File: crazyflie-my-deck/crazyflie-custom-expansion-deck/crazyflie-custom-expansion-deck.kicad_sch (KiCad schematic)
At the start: 3 parts, among them J1 Conn_01x10, J2 Conn_02x10_Odd_Even, J3 Conn_01x10

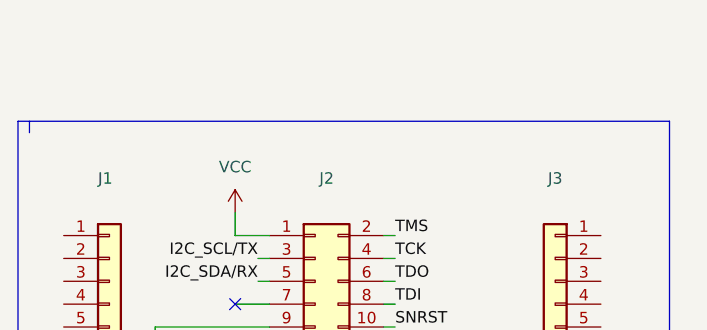
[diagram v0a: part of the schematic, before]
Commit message: [add] boost voltage
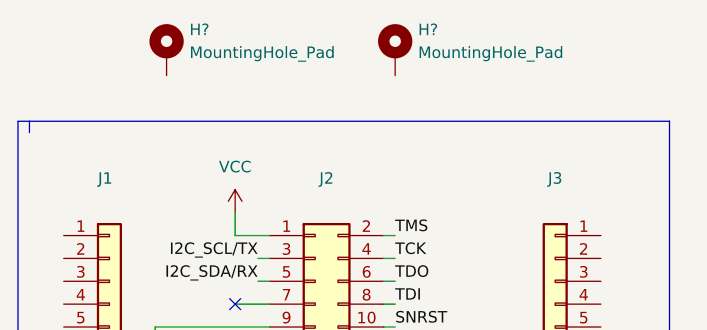
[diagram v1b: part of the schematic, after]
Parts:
- added H? (x2): MountingHole_Pad, symbol Mechanical:MountingHole_Pad
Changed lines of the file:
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@@
+    (pin "1")
+  )
+  (symbol (lib_id "Mechanical:MountingHole_Pad") (at 151.13 66.04 0) (unit 1)
+    (in_bom yes) (on_board yes) (fields_autoplaced)
+    (property "Reference" "H?" (id 0) (at 153.67 63.4999 0)
+      (effects (font (size 1.27 1.27)) (justify left))
+    )
+    (property "Value" "MountingHole_Pad" (id 1) (at 153.67 66.0399 0)
+      (effects (font (size 1.27 1.27)) (justify left))
+    )
+    (property "Footprint" "" (id 2) (at 151.13 66.04 0)
+      (effects (font (size 1.27 1.27)) hide)
+    )
+    (property "Datasheet" "~" (id 3) (at 151.13 66.04 0)
+      (effects (font (size 1.27 1.27)) hide)
+    )
     (pin "1")
   )
@@
     (pin "1")
   )
+  (symbol (lib_id "Mechanical:MountingHole_Pad") (at 125.73 66.04 0) (unit 1)
+    (in_bom yes) (on_board yes) (fields_autoplaced)
+    (property "Reference" "H?" (id 0) (at 128.27 63.4999 0)
+      (effects (font (size 1.27 1.27)) (justify left))
+    )
+    (property "Value" "MountingHole_Pad" (id 1) (at 128.27 66.0399 0)
+      (effects (font (size 1.27 1.27)) (justify left))
+    )
+    (property "Footprint" "" (id 2) (at 125.73 66.04 0)
+      (effects (font (size 1.27 1.27)) hide)
+    )
+    (property "Datasheet" "~" (id 3) (at 125.73 66.04 0)
+      (effects (font (size 1.27 1.27)) hide)
+    )
+    (pin "1")
+  )
   (sheet_instances
     (path "/" (page "1"))
@@
       (reference "#PWR06") (unit 1) (value "GNDA") (footprint "")
     )
+    (path "/76a03ed3-762f-4d41-a0c5-8ca717b403a8"
+      (reference "H?") (unit 1) (value "MountingHole_Pad") (footprint "")
+    )
+    (path "/d9a65ee8-bd3a-49dd-a674-f61b61978027"
+      (reference "H?") (unit 1) (value "MountingHole_Pad") (footprint "")
+    )
     (path "/388ad4a6-c2ab-454b-ae40-8bf09ddb6eea"

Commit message: acomodo de componentes
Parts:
- removed J2: Conn_02x10_Odd_Even, Connector_PinHeader_1.27mm:PinHeader_2x10_P1.27mm_Vertical, symbol Connector_Generic:Conn_02x10_Odd_Even
- added C1, C4: C_Polarized, Capacitor_Tantalum_SMD:CP_EIA-3528-15_AVX-H, symbol Device:C_Polarized
- added C2: C_Polarized, Capacitor_SMD:C_0805_2012Metric, symbol Device:C_Polarized
- added C3: C_Polarized, Capacitor_SMD:C_1210_3225Metric, symbol Device:C_Polarized
- added D1: 1SS355VM, Diode_SMD:D_SOD-323F, symbol Diode:1SS355VM
- added J2: Conn_01x06_Male, Connector_PinHeader_1.27mm:PinHeader_1x06_P1.27mm_Horizontal, symbol Connector:Conn_01x06_Male
- added L1: L, Inductor_SMD:L_1210_3225Metric, symbol Device:L
- added R1, R2, R3, R4: R, Resistor_SMD:R_0805_2012Metric, symbol Device:R
- added U1: MAX712CSE, Package_SO:SOIC-16_3.9x9.9mm_P1.27mm, symbol Battery_Management:MAX712CSE
- gave numbers to parts that had none: 2
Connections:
- net GND: now also C1.2, C2.2, C3.2, C4.2, J2.2 (Pin_2), R2.2, R4.2
- new net: R3.2, R4.1
- new net: C1.1, J2.1 (Pin_1), L1.1, R1.1
- new net: D1.2 (A), L1.2
- new net: R1.2, R2.1
- new net: C4.1, D1.1 (K)
- no-connect marks 1 -> 0
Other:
- moved on the sheet: H1, H2, J1, J3

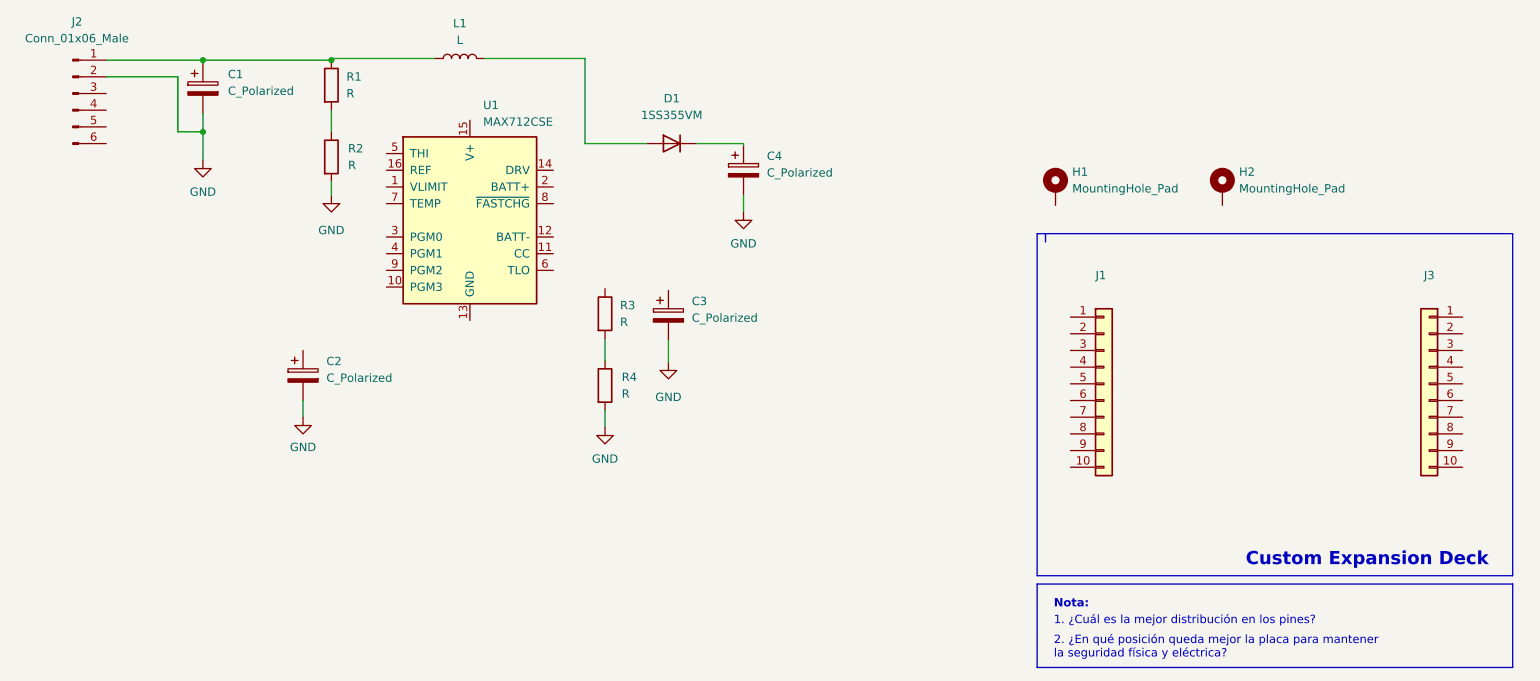
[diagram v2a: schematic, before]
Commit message: Schematics for Voltage Booster
Connections and change of pins for MAX711
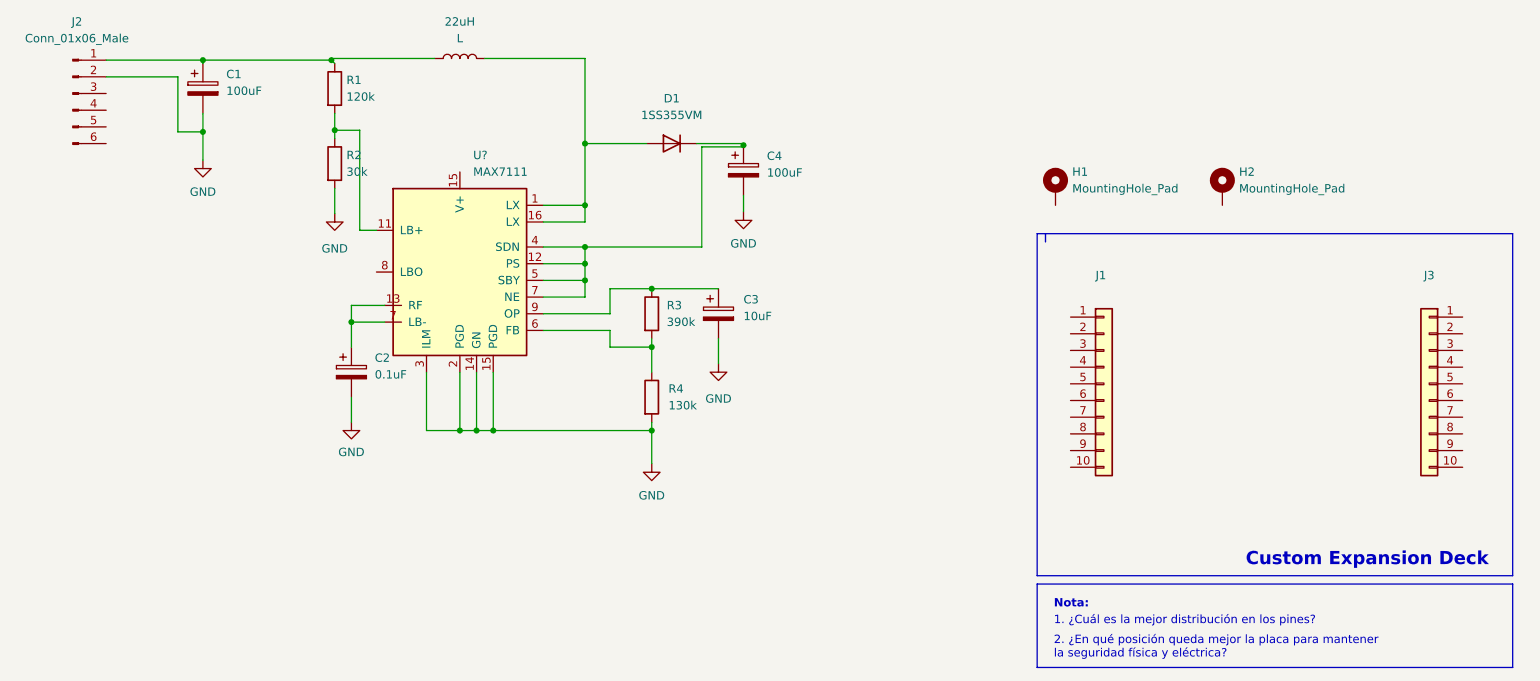
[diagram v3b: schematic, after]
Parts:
- removed U1: MAX712CSE, Package_SO:SOIC-16_3.9x9.9mm_P1.27mm, symbol Battery_Management:MAX712CSE
- added U?: MAX7111, Package_SO:SOIC-16_3.9x9.9mm_P1.27mm, symbol Battery_Management:MAX7111
- C1, C4: value C_Polarized -> 100uF
- C2: value C_Polarized -> 0.1uF
- C3: value C_Polarized -> 10uF
- R1: value R -> 120k
- R2: value R -> 30k
- R3: value R -> 390k
- R4: value R -> 130k
- renumbered L1 to 22uH
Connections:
- net GND: now also U?.14 (GN), U?.15 (V+), U?.2 (PGD), U?.3 (ILM)
- net at R3.1: now also C3.1, U?.9 (OP)
- net at R3.2, R4.1: now also U?.6 (FB)
- net at 22uH.2, D1.2 (A): now also U?.1 (LX), U?.16 (LX)
- net at R1.2, R2.1: now also U?.11 (LB+)
- net at C4.1, D1.1 (K): now also U?.12 (PS), U?.4 (SDN), U?.5 (SBY), U?.7 (NE)
- net at C2.1: now also U?.13 (RF), U?.7 (NE)
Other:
- moved on the sheet: C2, C3, R1, R2, R3, R4

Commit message: Fixes
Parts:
- removed U?: MAX7111, Package_SO:SOIC-16_3.9x9.9mm_P1.27mm, symbol Battery_Management:MAX7111
- added U1: MAX7111, Package_SO:SOIC-16_3.9x9.9mm_P1.27mm, symbol Battery_Management:MAX7111
- renumbered 22uH to 22uH1
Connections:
- net GND: now also U1.14 (GN), U1.15 (V+), U1.2 (PGD), U1.3 (ILM)
- net at C3.1, R3.1: now also U1.9 (OP)
- net at R3.2, R4.1: now also U1.6 (FB)
- net at 22uH1.2, D1.2 (A): now also U1.1 (LX), U1.16 (LX)
- net at R1.2, R2.1: now also U1.11 (LB+)
- net at C4.1, D1.1 (K): now also U1.12 (PS), U1.4 (SDN), U1.5 (SBY), U1.7 (NE)
- net at C2.1: now also U1.10 (LB-), U1.13 (RF)
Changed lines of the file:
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@@
     (pin "1")
+  )
+  (symbol (lib_id "Battery_Management:MAX7111") (at 90.17 97.79 0) (unit 1)
+    (in_bom yes) (on_board yes) (fields_autoplaced)
+    (property "Reference" "U1" (id 0) (at 92.1894 80.01 0)
+      (effects (font (size 1.27 1.27)) (justify left))
+    )
+    (property "Value" "MAX7111" (id 1) (at 92.1894 82.55 0)
+      (effects (font (size 1.27 1.27)) (justify left))
+    )
+    (property "Footprint" "Package_SO:SOIC-16_3.9x9.9mm_P1.27mm" (id 2) (at 90.17 115.57 0)
+      (effects (font (size 1.27 1.27)) hide)
+    )
+    (property "Datasheet" "https://datasheets.maximintegrated.com/en/ds/MAX712-MAX713.pdf" (id 3) (at 72.39 80.01 0)
+      (effects (font (size 1.27 1.27)) hide)
+    )
+    (pin "1")
+    (pin "11")
+    (pin "12")
+    (pin "13")
+    (pin "14")
+    (pin "15")
+    (pin "15")
+    (pin "16")
+    (pin "2")
+    (pin "3")
+    (pin "4")
+    (pin "5")
+    (pin "6")
+    (pin "10")
+    (pin "7")
+    (pin "8")
+    (pin "9")
   )
   (symbol (lib_id "Connector_Generic:Conn_01x10") (at 188.214 114.808 0) (unit 1)
@@
   (symbol (lib_id "Device:L") (at 90.17 65.278 90) (unit 1)
     (in_bom yes) (on_board yes) (fields_autoplaced)
-    (property "Reference" "22uH" (id 0) (at 90.17 59.69 90))
+    (property "Reference" "22uH1" (id 0) (at 90.17 59.69 90))
     (property "Value" "L" (id 1) (at 90.17 62.23 90))
     (property "Footprint" "Inductor_SMD:L_1210_3225Metric" (id 2) (at 90.17 65.278 0)
@@
     )
     (pin "1")
-  )
-  (symbol (lib_id "Battery_Management:MAX7111") (at 90.17 97.79 0) (unit 1)
-    (in_bom yes) (on_board yes) (fields_autoplaced)
-    (property "Reference" "U?" (id 0) (at 92.1894 80.01 0)
-      (effects (font (size 1.27 1.27)) (justify left))
-    )
-    (property "Value" "MAX7111" (id 1) (at 92.1894 82.55 0)
-      (effects (font (size 1.27 1.27)) (justify left))
-    )
-    (property "Footprint" "Package_SO:SOIC-16_3.9x9.9mm_P1.27mm" (id 2) (at 90.17 115.57 0)
-      (effects (font (size 1.27 1.27)) hide)
-    )
-    (property "Datasheet" "https://datasheets.maximintegrated.com/en/ds/MAX712-MAX713.pdf" (id 3) (at 72.39 80.01 0)
-      (effects (font (size 1.27 1.27)) hide)
-    )
-    (pin "1")
-    (pin "11")
-    (pin "12")
-    (pin "13")
-    (pin "14")
-    (pin "15")
-    (pin "15")
-    (pin "16")
-    (pin "2")
-    (pin "3")
-    (pin "4")
-    (pin "5")
-    (pin "6")
-    (pin "7")
-    (pin "7")
-    (pin "9")
-    (pin "8")
   )
   (symbol (lib_id "Diode:1SS355VM") (at 122.428 78.232 0) (mirror y) (unit 1)
@@
     )
     (path "/63f68aae-215d-48f8-934a-2726f16762b6"
-      (reference "22uH") (unit 1) (value "L") (footprint "Inductor_SMD:L_1210_3225Metric")
+      (reference "22uH1") (unit 1) (value "L") (footprint "Inductor_SMD:L_1210_3225Metric")
     )
     (path "/4d3e9d1d-ce51-42ca-be59-2c77834705f0"
@@
       (reference "R4") (unit 1) (value "130k") (footprint "Resistor_SMD:R_0805_2012Metric")
     )
-    (path "/a28b1465-c59f-4464-af17-db4f1321b7fc"
-      (reference "U?") (unit 1) (value "MAX7111") (footprint "Package_SO:SOIC-16_3.9x9.9mm_P1.27mm")
-    )
-  )
+    (path "/32370ee8-91f4-40c5-9f1f-b1b5884d4ee2"
+      (reference "U1") (unit 1) (value "MAX7111") (footprint "Package_SO:SOIC-16_3.9x9.9mm_P1.27mm")
+    )
+  )
